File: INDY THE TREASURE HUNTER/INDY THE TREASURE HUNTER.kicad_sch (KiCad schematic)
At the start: 4 parts, among them J1 Conn_01x06_Pin, J2 Conn_01x06_Pin, J3 Conn_01x06_Pin, J6 Conn_01x06_Pin

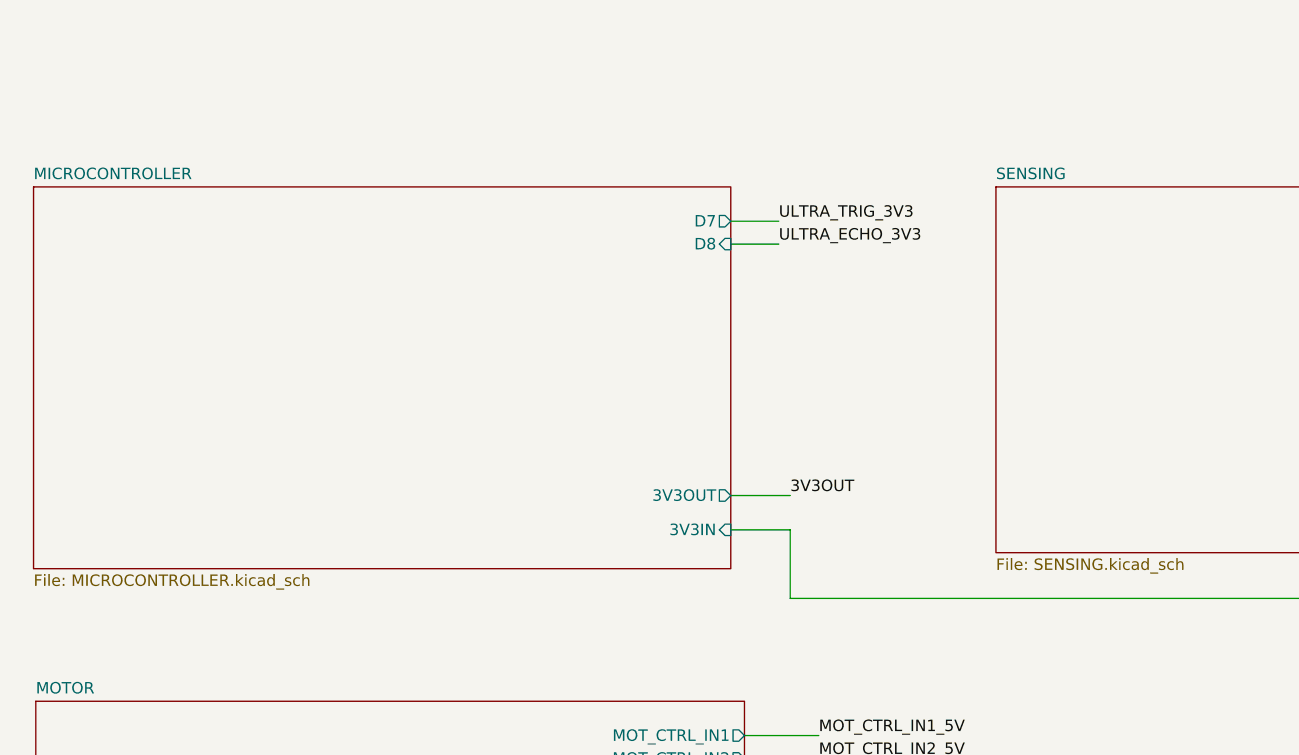
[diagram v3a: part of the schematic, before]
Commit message: Line sensor data lines configured
Im pretty sure the line sensors operate fine on 3v3, so no need to shift their logic levels or anything
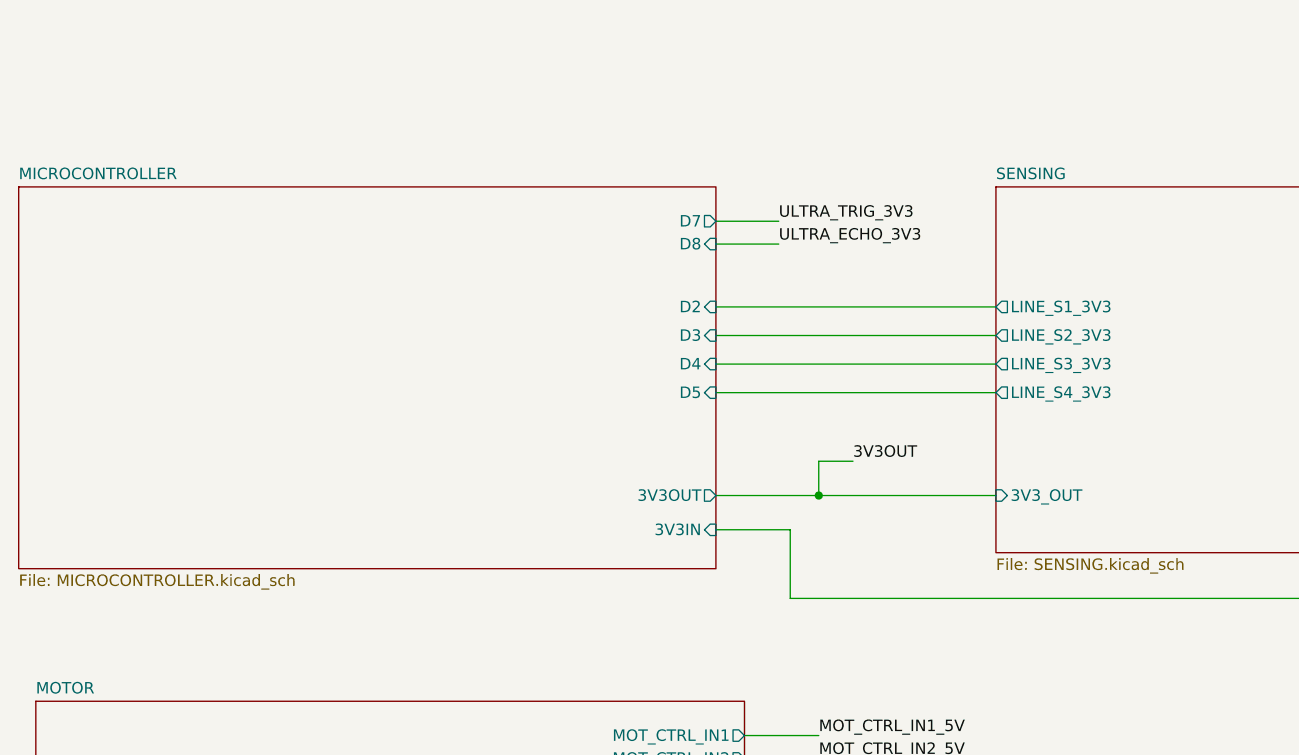
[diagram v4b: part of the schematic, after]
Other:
- sheet MICROCONTROLLER ports: added D2, D3, D4, D5; removed none
- sheet SENSING ports: added 3V3_OUT, LINE_S1_3V3, LINE_S2_3V3, LINE_S3_3V3, LINE_S4_3V3; removed none
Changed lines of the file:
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@@
   (junction (at 189.23 114.3) (diameter 0) (color 0 0 0 0)
   )
+  (junction (at 106.045 80.01) (diameter 0) (color 0 0 0 0)
+  )
   (wire (pts (xy 240.665 36.195) (xy 240.665 33.655))
     (stroke (width 0) (type default))
@@
     (stroke (width 0) (type default))
   )
-  (wire (pts (xy 96.266 80.01) (xy 102.87 80.01))
-    (stroke (width 0) (type default))
-  )
   (wire (pts (xy 260.35 36.195) (xy 264.795 36.195))
     (stroke (width 0) (type default))
@@
     (stroke (width 0) (type default))
   )
+  (wire (pts (xy 94.615 68.58) (xy 125.73 68.58))
+    (stroke (width 0) (type default))
+  )
   (wire (pts (xy 79.375 163.195) (xy 189.23 163.195))
     (stroke (width 0) (type default))
@@
     (stroke (width 0) (type default))
   )
+  (wire (pts (xy 94.615 59.055) (xy 125.73 59.055))
+    (stroke (width 0) (type default))
+  )
   (wire (pts (xy 260.35 31.115) (xy 271.78 31.115))
     (stroke (width 0) (type default))
@@
     (stroke (width 0) (type default))
   )
+  (wire (pts (xy 94.615 65.405) (xy 125.73 65.405))
+    (stroke (width 0) (type default))
+  )
   (wire (pts (xy 210.185 31.115) (xy 210.185 33.655))
     (stroke (width 0) (type default))
@@
     (stroke (width 0) (type default))
   )
-  (wire (pts (xy 96.266 52.07) (xy 101.6 52.07))
+  (wire (pts (xy 94.615 52.07) (xy 101.6 52.07))
     (stroke (width 0) (type default))
   )
@@
     (stroke (width 0) (type default))
   )
+  (wire (pts (xy 106.045 76.2) (xy 109.855 76.2))
+    (stroke (width 0) (type default))
+  )
+  (wire (pts (xy 94.615 62.23) (xy 125.73 62.23))
+    (stroke (width 0) (type default))
+  )
   (wire (pts (xy 240.03 23.495) (xy 245.11 23.495))
     (stroke (width 0) (type default))
@@
     (stroke (width 0) (type default))
   )
-  (wire (pts (xy 102.87 83.82) (xy 96.266 83.82))
+  (wire (pts (xy 102.87 83.82) (xy 94.615 83.82))
     (stroke (width 0) (type default))
   )
@@
     (stroke (width 0) (type default))
   )
+  (wire (pts (xy 94.615 80.01) (xy 106.045 80.01))
+    (stroke (width 0) (type default))
+  )
   (wire (pts (xy 79.375 158.115) (xy 181.61 158.115))
     (stroke (width 0) (type default))
@@
     (stroke (width 0) (type default))
   )
-  (wire (pts (xy 96.266 49.53) (xy 101.6 49.53))
+  (wire (pts (xy 94.615 49.53) (xy 101.6 49.53))
     (stroke (width 0) (type default))
   )
@@
     (stroke (width 0) (type default))
   )
+  (wire (pts (xy 106.045 80.01) (xy 125.73 80.01))
+    (stroke (width 0) (type default))
+  )
   (wire (pts (xy 241.3 28.575) (xy 245.11 28.575))
     (stroke (width 0) (type default))
   )
+  (wire (pts (xy 106.045 76.2) (xy 106.045 80.01))
+    (stroke (width 0) (type default))
+  )
   (text "Logic level converter 1" (at 182.245 14.605 0)
     (effects (font (size 1.27 1.27)) (justify left bottom))
@@
     (effects (font (size 1.27 1.27)) (justify left bottom))
   )
-  (label "3V3OUT" (at 102.87 80.01 0) (fields_autoplaced)
+  (label "3V3OUT" (at 109.855 76.2 0) (fields_autoplaced)
     (effects (font (size 1.27 1.27)) (justify left bottom))
   )
@@
       (effects (font (size 1.27 1.27)) (justify right))
     )
+    (pin "3V3_OUT" input (at 125.73 80.01 180)
+      (effects (font (size 1.27 1.27)) (justify left))
+    )
+    (pin "LINE_S1_3V3" output (at 125.73 59.055 180)
+      (effects (font (size 1.27 1.27)) (justify left))
+    )
+    (pin "LINE_S2_3V3" output (at 125.73 62.23 180)
+      (effects (font (size 1.27 1.27)) (justify left))
+    )
+    (pin "LINE_S3_3V3" output (at 125.73 65.405 180)
+      (effects (font (size 1.27 1.27)) (justify left))
+    )
+    (pin "LINE_S4_3V3" output (at 125.73 68.58 180)
+      (effects (font (size 1.27 1.27)) (justify left))
+    )
     (instances
       (project "INDY THE TREASURE HUNTER"
@@
     )
   )
-  (sheet (at 18.796 45.72) (size 77.47 42.418) (fields_autoplaced)
+  (sheet (at 17.145 45.72) (size 77.47 42.418) (fields_autoplaced)
     (stroke (width 0.1524) (type solid))
     (fill (color 0 0 0 0.0000))
-    (property "Sheetname" "MICROCONTROLLER" (at 18.796 45.0084 0)
+    (property "Sheetname" "MICROCONTROLLER" (at 17.145 45.0084 0)
       (effects (font (size 1.27 1.27)) (justify left bottom))
     )
-    (property "Sheetfile" "MICROCONTROLLER.kicad_sch" (at 18.796 88.7226 0)
+    (property "Sheetfile" "MICROCONTROLLER.kicad_sch" (at 17.145 88.7226 0)
       (effects (font (size 1.27 1.27)) (justify left top))
     )
-    (pin "3V3IN" input (at 96.266 83.82 0)
-      (effects (font (size 1.27 1.27)) (justify right))
-    )
-    (pin "3V3OUT" output (at 96.266 80.01 0)
-      (effects (font (size 1.27 1.27)) (justify right))
-    )
-    (pin "D8" input (at 96.266 52.07 0)
-      (effects (font (size 1.27 1.27)) (justify right))
-    )
-    (pin "D7" output (at 96.266 49.53 0)
-      (effects (font (size 1.27 1.27)) (justify right))
-    )
+    (pin "3V3IN" input (at 94.615 83.82 0)
+      (effects (font (size 1.27 1.27)) (justify right))
+    )
+    (pin "3V3OUT" output (at 94.615 80.01 0)
+      (effects (font (size 1.27 1.27)) (justify right))
+    )
+    (pin "D8" input (at 94.615 52.07 0)
+      (effects (font (size 1.27 1.27)) (justify right))
+    )
+    (pin "D7" output (at 94.615 49.53 0)
+      (effects (font (size 1.27 1.27)) (justify right))
+    )
+    (pin "D2" input (at 94.615 59.055 0)
+      (effects (font (size 1.27 1.27)) (justify right))
+    )
+    (pin "D3" input (at 94.615 62.23 0)
+      (effects (font (size 1.27 1.27)) (justify right))
+    )
+    (pin "D4" input (at 94.615 65.405 0)
+      (effects (font (size 1.27 1.27)) (justify right))
+    )
+    (pin "D5" input (at 94.615 68.58 0)
+      (effects (font (size 1.27 1.27)) (justify right))
+    )

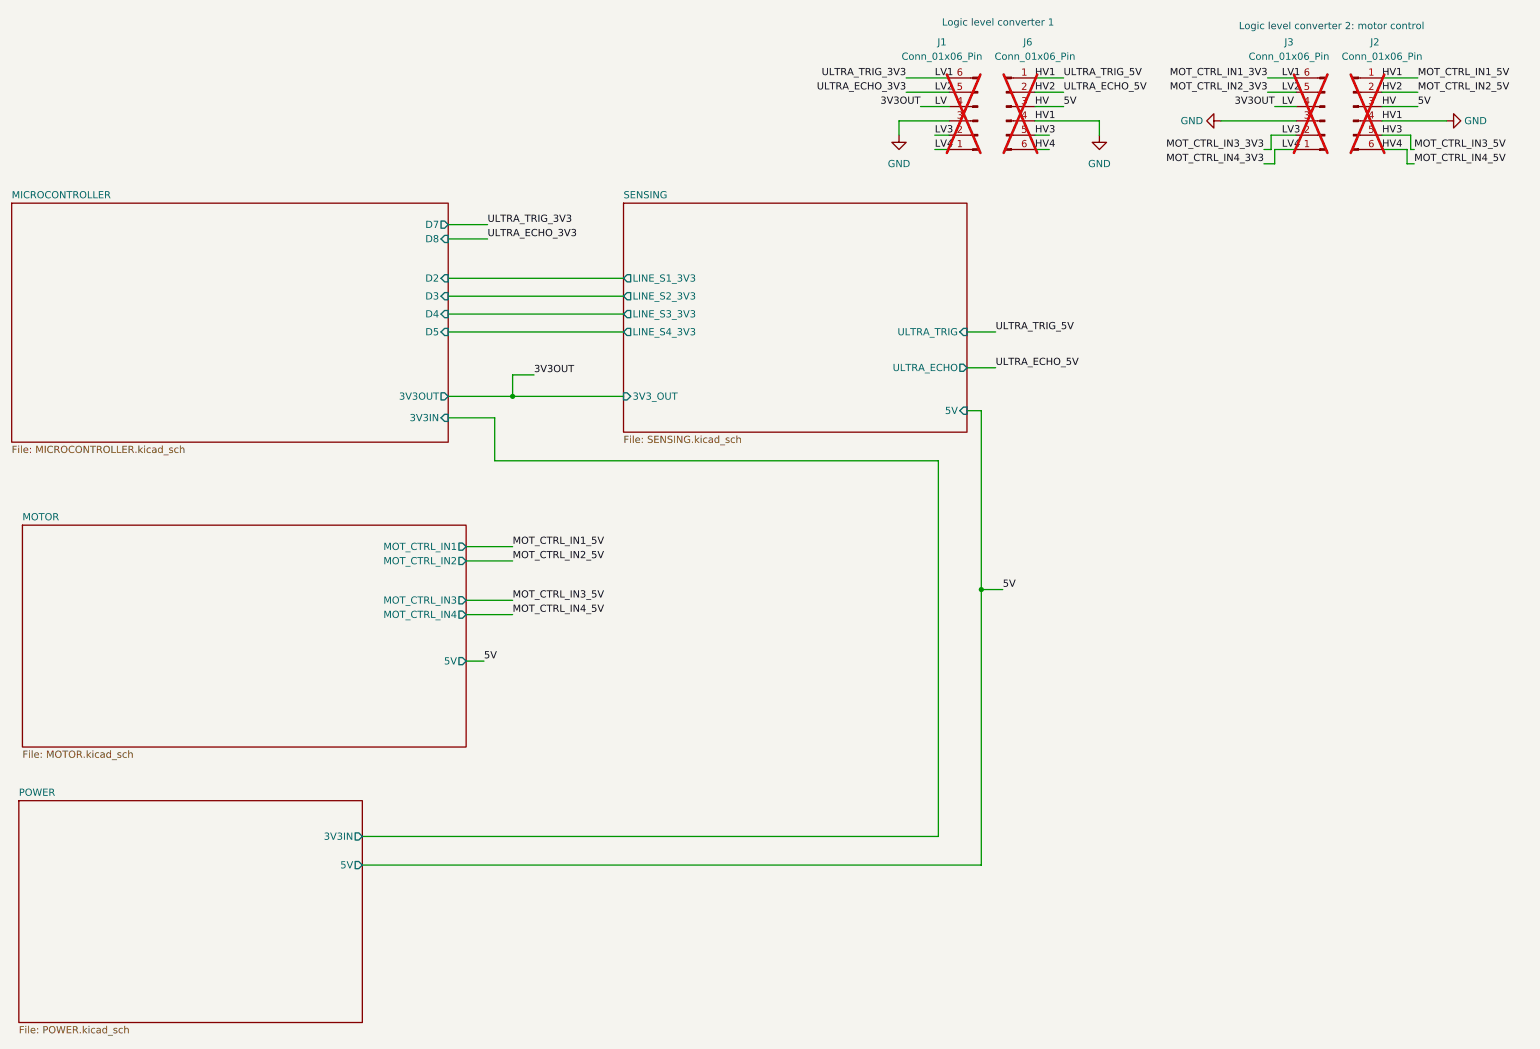
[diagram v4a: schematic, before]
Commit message: Neatened up schematic for milestone 1 handin
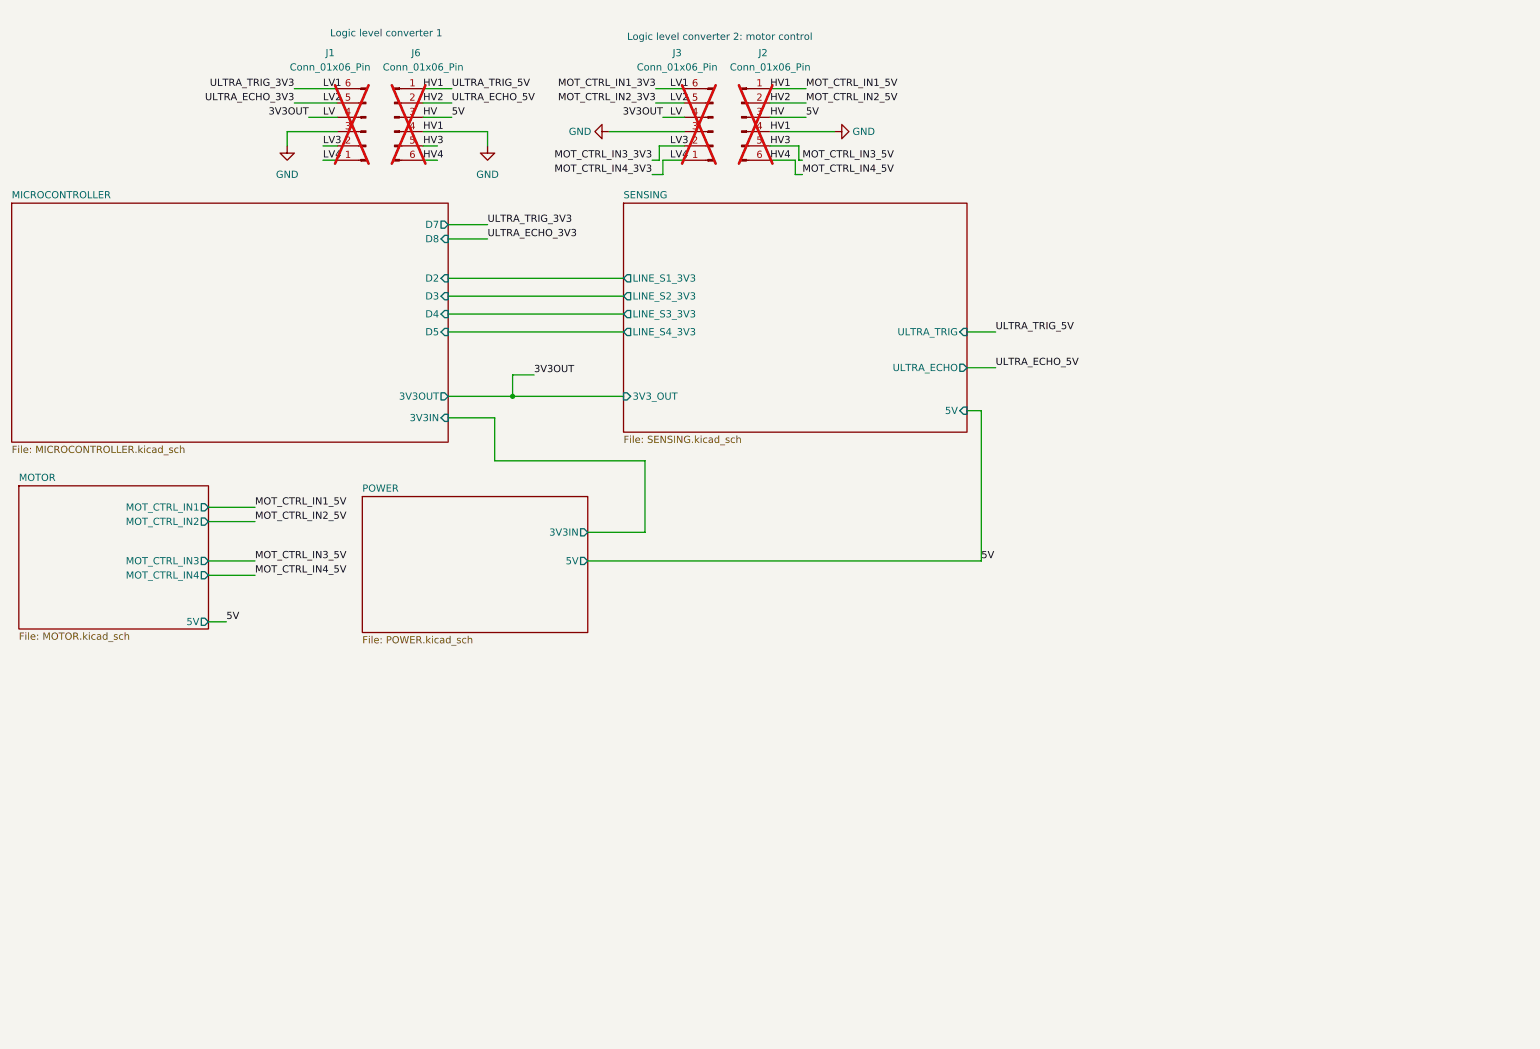
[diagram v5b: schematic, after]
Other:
- moved on the sheet: J1, J2, J3, J6

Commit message: No 3V3 regulator
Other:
- sheet MICROCONTROLLER ports: added 5V; removed 3V3IN
- sheet POWER ports: added none; removed 3V3IN
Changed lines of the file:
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@@
 (kicad_sch (version 20230121) (generator eeschema)
   (paper "A4")
+  (junction (at 126.365 109.22) (diameter 0) (color 0 0 0 0)
+  )
   (junction (at 106.045 80.01) (diameter 0) (color 0 0 0 0)
   )
@@
     (stroke (width 0) (type default))
   )
-  (wire (pts (xy 129.54 104.14) (xy 129.54 91.44))
-    (stroke (width 0) (type default))
-  )
   (wire (pts (xy 151.765 38.1) (xy 156.21 38.1))
     (stroke (width 0) (type default))
@@
     (stroke (width 0) (type default))
   )
-  (wire (pts (xy 102.87 91.44) (xy 129.54 91.44))
-    (stroke (width 0) (type default))
-  )
   (wire (pts (xy 131.445 27.94) (xy 136.525 27.94))
     (stroke (width 0) (type default))
@@
     (stroke (width 0) (type default))
   )
+  (wire (pts (xy 126.365 90.805) (xy 114.935 90.805))
+    (stroke (width 0) (type default))
+  )
   (wire (pts (xy 94.615 68.58) (xy 125.73 68.58))
     (stroke (width 0) (type default))
@@
     (stroke (width 0) (type default))
   )
+  (wire (pts (xy 114.935 85.725) (xy 94.615 85.725))
+    (stroke (width 0) (type default))
+  )
+  (wire (pts (xy 126.365 109.22) (xy 126.365 90.805))
+    (stroke (width 0) (type default))
+  )
   (wire (pts (xy 72.39 35.56) (xy 74.93 35.56))
     (stroke (width 0) (type default))
@@
     (stroke (width 0) (type default))
   )
-  (wire (pts (xy 119.38 104.14) (xy 129.54 104.14))
+  (wire (pts (xy 126.365 109.22) (xy 189.23 109.22))
     (stroke (width 0) (type default))
   )
@@
     (stroke (width 0) (type default))
   )
-  (wire (pts (xy 119.38 109.22) (xy 189.23 109.22))
+  (wire (pts (xy 119.38 109.22) (xy 126.365 109.22))
     (stroke (width 0) (type default))
   )
@@
     (stroke (width 0) (type default))
   )
+  (wire (pts (xy 114.935 90.805) (xy 114.935 85.725))
+    (stroke (width 0) (type default))
+  )
   (wire (pts (xy 52.07 120.015) (xy 55.245 120.015))
-    (stroke (width 0) (type default))
-  )
-  (wire (pts (xy 102.87 91.44) (xy 102.87 83.82))
-    (stroke (width 0) (type default))
-  )
-  (wire (pts (xy 102.87 83.82) (xy 94.615 83.82))
     (stroke (width 0) (type default))
   )
@@
       (effects (font (size 1.27 1.27)) (justify left top))
     )
-    (pin "3V3IN" input (at 94.615 83.82 0)
-      (effects (font (size 1.27 1.27)) (justify right))
-    )
     (pin "3V3OUT" output (at 94.615 80.01 0)
       (effects (font (size 1.27 1.27)) (justify right))
@@
     )
     (pin "D5" input (at 94.615 68.58 0)
+      (effects (font (size 1.27 1.27)) (justify right))
+    )
+    (pin "5V" input (at 94.615 85.725 0)
       (effects (font (size 1.27 1.27)) (justify right))
     )
@@
       (effects (font (size 1.27 1.27)) (justify right))
     )
-    (pin "3V3IN" output (at 119.38 104.14 0)
-      (effects (font (size 1.27 1.27)) (justify right))
-    )
